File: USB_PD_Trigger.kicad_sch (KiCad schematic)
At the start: 53 parts, among them J1 Conn_02x08_Odd_Even, J2 Conn_02x08_Odd_Even, J3 Conn_01x02, U1 AP33771C, U2 HP8KB7TB1, X1 2171790001, X2 Screw_Terminal_01x02

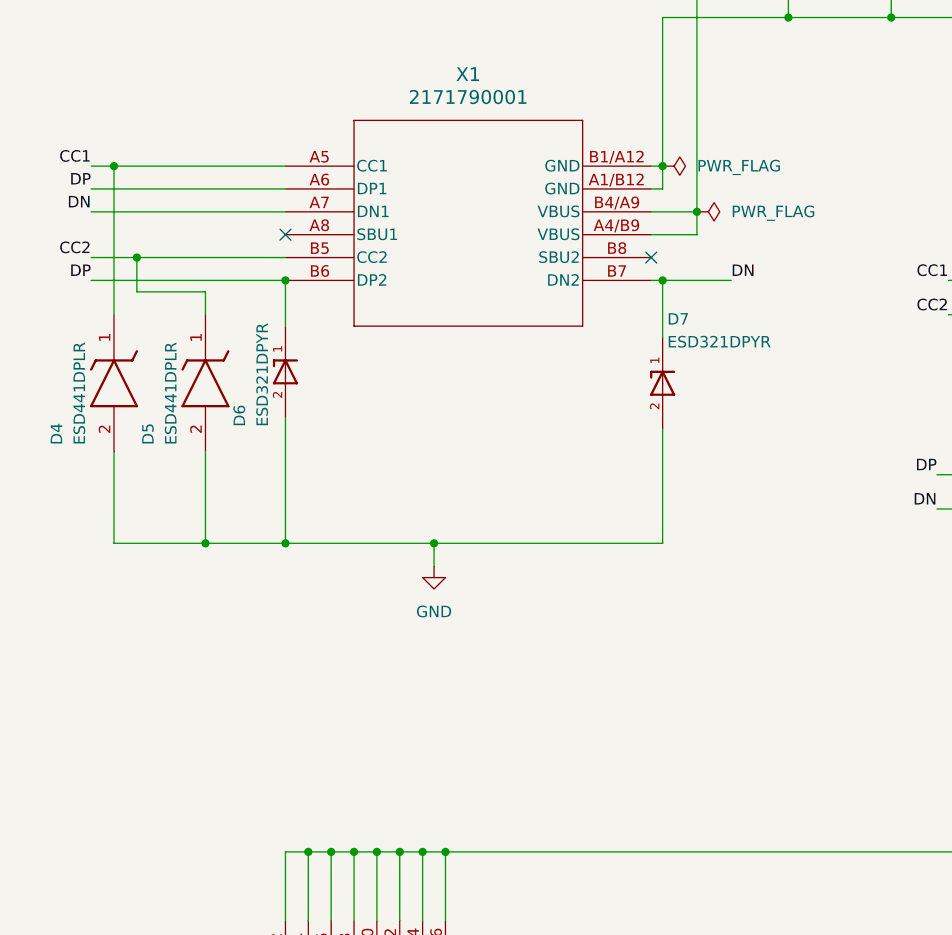
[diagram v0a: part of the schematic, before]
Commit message: added stitching vias and changed ESD diodes
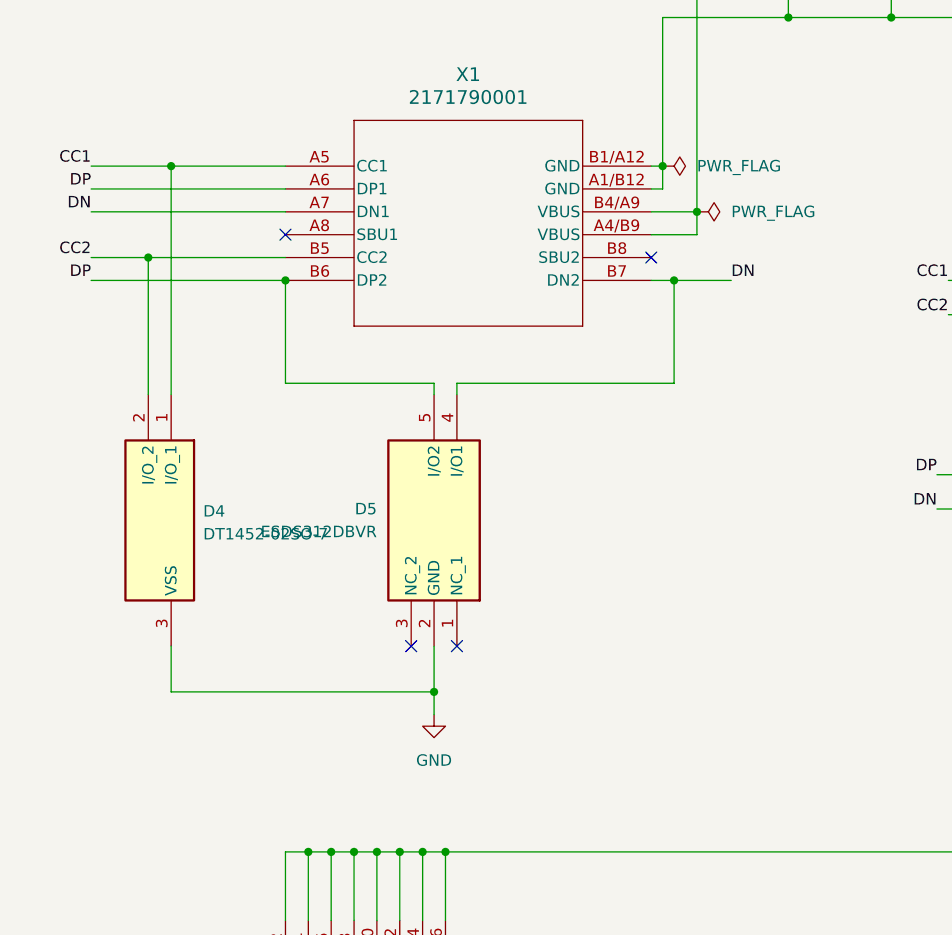
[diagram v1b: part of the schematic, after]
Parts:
- removed D4, D5: ESD441DPLR, footprints:ESD441DPLR, symbol ESD441DPLR:ESD441DPLR
- removed D6, D7: ESD321DPYR, footprints:ESD321DPYR, symbol ESD321DPYR:ESD321DPYR
- added D4: DT1452-02SO-7, footprints:DT1452-02SO-7, symbol DT1452-02SO-7:DT1452-02SO-7
- added D5: ESDS312DBVR, footprints:ESDS312DBVR, symbol ESDS312DBVR:ESDS312DBVR
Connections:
- net CC1: now also D4.1 (I/O_1)
- net CC2: now also D4.2 (I/O_2)
- net DN: now also D5.4 (I/O1)
- net DP: now also D5.5 (I/O2)
- net GND: now also D4.3 (VSS), D5.2 (GND)
- no-connect marks 2 -> 4
